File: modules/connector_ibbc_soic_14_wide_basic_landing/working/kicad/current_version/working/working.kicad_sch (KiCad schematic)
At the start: 1 part, among them U1 insoic14wi2cland

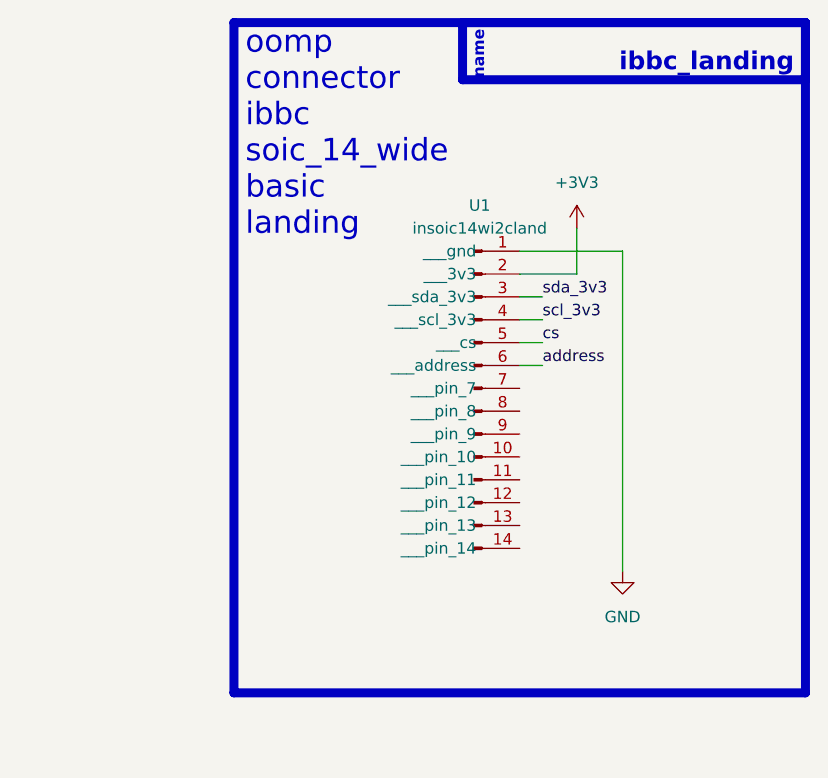
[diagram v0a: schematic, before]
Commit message: fixed formatting to be more consistent
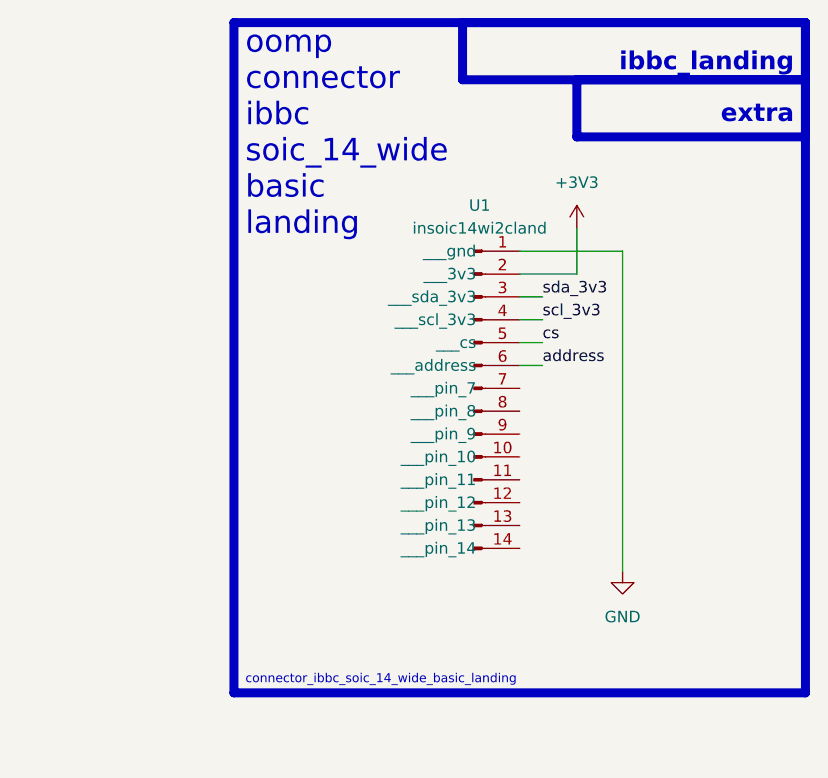
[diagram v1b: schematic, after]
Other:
- note added: "connector_ibbc_soic_14_wide_basic_landing"
- note added: "extra"
- note removed: "name"
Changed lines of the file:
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@@
     (stroke (width 0) (type default))
+  )
+  (rectangle (start 132.08 24.13) (end 157.48 30.48)
+    (stroke (width 1) (type default))
+    (fill (type none))
   )
   (rectangle (start 93.98 17.78) (end 157.48 92.2532)
@@
   (rectangle (start 119.38 17.78) (end 157.48 24.13)
     (stroke (width 1) (type default))
-    (fill (type color) (color 0 0 0 0))
+    (fill (type none))
+  )
+  (text "connector_ibbc_soic_14_wide_basic_landing" (at 95.25 91.44 0)
+    (effects (font (size 1 1)) (justify left bottom))
   )
   (text "ibbc_landing\n\n" (at 156.21 26.67 0)
-    (effects (font (size 2 2) (thickness 0.8) bold (color 255 255 255 1)) (justify right bottom))
-  )
-  (text "name" (at 121.92 24.13 90)
-    (effects (font (size 1.27 1.27) (thickness 0.254) bold (color 255 255 255 1)) (justify left bottom))
+    (effects (font (size 2 2) (thickness 0.8) bold) (justify right bottom))
   )
   (text "oomp\nconnector\nibbc\nsoic_14_wide\nbasic\nlanding\n\n" (at 95.25 45.72 0)
     (effects (font (size 2.5 2.5)) (justify left bottom))
   )
+  (text "extra" (at 156.21 29.21 0)
+    (effects (font (size 2 2) (thickness 0.8) bold) (justify right bottom))
+  )
   (label "cs" (at 128.27 53.34 0) (fields_autoplaced)

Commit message: schematic formatting
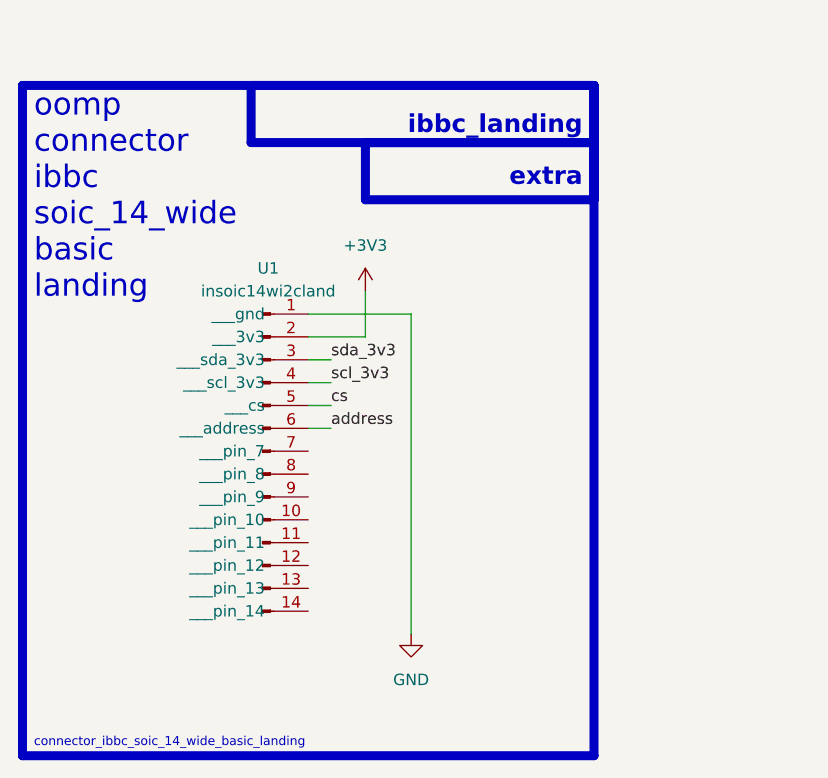
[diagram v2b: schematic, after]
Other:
- moved on the sheet: U1
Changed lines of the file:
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@@
 (kicad_sch (version 20230121) (generator eeschema)
-  (paper "A4")
-  (wire (pts (xy 125.73 43.18) (xy 137.16 43.18))
+  (paper "A5")
+  (wire (pts (xy 102.235 50.165) (xy 113.665 50.165))
     (stroke (width 0) (type default))
   )
-  (wire (pts (xy 132.08 45.72) (xy 132.08 40.64))
+  (wire (pts (xy 108.585 52.705) (xy 108.585 47.625))
     (stroke (width 0) (type default))
   )
-  (wire (pts (xy 125.73 50.8) (xy 128.27 50.8))
+  (wire (pts (xy 102.235 57.785) (xy 104.775 57.785))
     (stroke (width 0) (type default))
   )
-  (wire (pts (xy 125.73 53.34) (xy 128.27 53.34))
+  (wire (pts (xy 102.235 60.325) (xy 104.775 60.325))
     (stroke (width 0) (type default))
   )
-  (wire (pts (xy 125.73 45.72) (xy 132.08 45.72))
+  (wire (pts (xy 102.235 52.705) (xy 108.585 52.705))
     (stroke (width 0) (type default))
   )
-  (wire (pts (xy 125.73 48.26) (xy 128.27 48.26))
+  (wire (pts (xy 102.235 55.245) (xy 104.775 55.245))
     (stroke (width 0) (type default))
   )
-  (wire (pts (xy 137.16 43.18) (xy 137.16 78.74))
+  (wire (pts (xy 113.665 50.165) (xy 113.665 85.725))
     (stroke (width 0) (type default))
   )
-  (wire (pts (xy 125.73 55.88) (xy 128.27 55.88))
+  (wire (pts (xy 102.235 62.865) (xy 104.775 62.865))
     (stroke (width 0) (type default))
   )
-  (rectangle (start 132.08 24.13) (end 157.48 30.48)
+  (rectangle (start 108.585 31.115) (end 133.985 37.465)
     (stroke (width 1) (type default))
     (fill (type none))
   )
-  (rectangle (start 93.98 17.78) (end 157.48 92.2532)
+  (rectangle (start 70.485 24.765) (end 133.985 99.2382)
     (stroke (width 1) (type default))
     (fill (type none))
   )
-  (rectangle (start 119.38 17.78) (end 157.48 24.13)
+  (rectangle (start 95.885 24.765) (end 133.985 31.115)
     (stroke (width 1) (type default))
     (fill (type none))
   )
-  (text "connector_ibbc_soic_14_wide_basic_landing" (at 95.25 91.44 0)
+  (text "connector_ibbc_soic_14_wide_basic_landing" (at 71.755 98.425 0)
     (effects (font (size 1 1)) (justify left bottom))
   )
-  (text "ibbc_landing\n\n" (at 156.21 26.67 0)
+  (text "ibbc_landing\n\n" (at 132.715 33.655 0)
     (effects (font (size 2 2) (thickness 0.8) bold) (justify right bottom))
   )
-  (text "oomp\nconnector\nibbc\nsoic_14_wide\nbasic\nlanding\n\n" (at 95.25 45.72 0)
+  (text "oomp\nconnector\nibbc\nsoic_14_wide\nbasic\nlanding\n\n" (at 71.755 52.705 0)
     (effects (font (size 2.5 2.5)) (justify left bottom))
   )
-  (text "extra" (at 156.21 29.21 0)
+  (text "extra" (at 132.715 36.195 0)
     (effects (font (size 2 2) (thickness 0.8) bold) (justify right bottom))
   )
-  (label "cs" (at 128.27 53.34 0) (fields_autoplaced)
+  (label "cs" (at 104.775 60.325 0) (fields_autoplaced)
     (effects (font (size 1.27 1.27)) (justify left bottom))
   )
-  (label "address" (at 128.27 55.88 0) (fields_autoplaced)
+  (label "address" (at 104.775 62.865 0) (fields_autoplaced)
     (effects (font (size 1.27 1.27)) (justify left bottom))
   )
-  (label "sda_3v3" (at 128.27 48.26 0) (fields_autoplaced)
+  (label "sda_3v3" (at 104.775 55.245 0) (fields_autoplaced)
     (effects (font (size 1.27 1.27)) (justify left bottom))
   )
-  (label "scl_3v3" (at 128.27 50.8 0) (fields_autoplaced)
+  (label "scl_3v3" (at 104.775 57.785 0) (fields_autoplaced)
     (effects (font (size 1.27 1.27)) (justify left bottom))
   )
-  (symbol (lib_id "oomlout_oomp_part_symbols:insoic14wi2cland_electronic_interposer_soic_14_wide_i2c_landing") (at 120.65 58.42 0) (unit 1)
+  (symbol (lib_id "oomlout_oomp_part_symbols:insoic14wi2cland_electronic_interposer_soic_14_wide_i2c_landing") (at 97.155 65.405 0) (unit 1)
     (in_bom yes) (on_board yes) (dnp no) (fields_autoplaced)
-    (property "Reference" "U1" (at 121.285 38.1 0)
+    (property "Reference" "U1" (at 97.79 45.085 0)
       (effects (font (size 1.27 1.27)))
     )
-    (property "Value" "insoic14wi2cland" (at 121.285 40.64 0)
+    (property "Value" "insoic14wi2cland" (at 97.79 47.625 0)
       (effects (font (size 1.27 1.27)))
     )
-    (property "Footprint" "oomlout_oomp_part_footprints:insoic14wi2cland_electronic_interposer_soic_14_wide_i2c_landing" (at 120.65 58.42 0)
+    (property "Footprint" "oomlout_oomp_part_footprints:insoic14wi2cland_electronic_interposer_soic_14_wide_i2c_landing" (at 97.155 65.405 0)
       (effects (font (size 1.27 1.27)) hide)
     )
-    (property "Datasheet" "https://github.com/oomlout/oomlout_oomp_v3/parts/electronic_interposer_soic_14_wide_i2c_landing/datasheet.pdf" (at 120.65 58.42 0)
+    (property "Datasheet" "https://github.com/oomlout/oomlout_oomp_v3/parts/electronic_interposer_soic_14_wide_i2c_landing/datasheet.pdf" (at 97.155 65.405 0)
       (effects (font (size 1.27 1.27)) hide)
     )
@@
     )
   )
-  (symbol (lib_id "power:GND") (at 137.16 78.74 0) (unit 1)
+  (symbol (lib_id "power:GND") (at 113.665 85.725 0) (unit 1)
     (in_bom yes) (on_board yes) (dnp no) (fields_autoplaced)
-    (property "Reference" "#PWR06" (at 137.16 85.09 0)
+    (property "Reference" "#PWR06" (at 113.665 92.075 0)
       (effects (font (size 1.27 1.27)) hide)
     )
-    (property "Value" "GND" (at 137.16 83.82 0)
+    (property "Value" "GND" (at 113.665 90.805 0)
       (effects (font (size 1.27 1.27)))
     )
-    (property "Footprint" "" (at 137.16 78.74 0)
+    (property "Footprint" "" (at 113.665 85.725 0)
       (effects (font (size 1.27 1.27)) hide)
     )
-    (property "Datasheet" "" (at 137.16 78.74 0)
+    (property "Datasheet" "" (at 113.665 85.725 0)
       (effects (font (size 1.27 1.27)) hide)
     )
@@
     )
   )
-  (symbol (lib_id "power:+3V3") (at 132.08 40.64 0) (unit 1)
+  (symbol (lib_id "power:+3V3") (at 108.585 47.625 0) (unit 1)
     (in_bom yes) (on_board yes) (dnp no) (fields_autoplaced)
-    (property "Reference" "#PWR05" (at 132.08 44.45 0)
+    (property "Reference" "#PWR05" (at 108.585 51.435 0)
       (effects (font (size 1.27 1.27)) hide)
     )
-    (property "Value" "+3V3" (at 132.08 35.56 0)
+    (property "Value" "+3V3" (at 108.585 42.545 0)
       (effects (font (size 1.27 1.27)))
     )
-    (property "Footprint" "" (at 132.08 40.64 0)
+    (property "Footprint" "" (at 108.585 47.625 0)
       (effects (font (size 1.27 1.27)) hide)
     )
-    (property "Datasheet" "" (at 132.08 40.64 0)
+    (property "Datasheet" "" (at 108.585 47.625 0)
       (effects (font (size 1.27 1.27)) hide)
     )
